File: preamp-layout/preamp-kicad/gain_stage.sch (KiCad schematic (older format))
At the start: 0 parts

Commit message: general layout work
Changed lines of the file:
@@
 $Descr A4 11693 8268
 encoding utf-8
-Sheet 11 11
+Sheet 13 13
 Title ""
 Date ""
@@
 Text HLabel 8050 3000 2    50   UnSpc ~ 0
 out_R
+Text HLabel 5700 4250 0    50   Output ~ 0
+MISO
+Text HLabel 5700 4400 0    50   Input ~ 0
+MOSI
+Text HLabel 5700 4550 0    50   Input ~ 0
+CLK
+Text HLabel 5700 4700 0    50   Input ~ 0
+CS_VOL
 $EndSCHEMATC

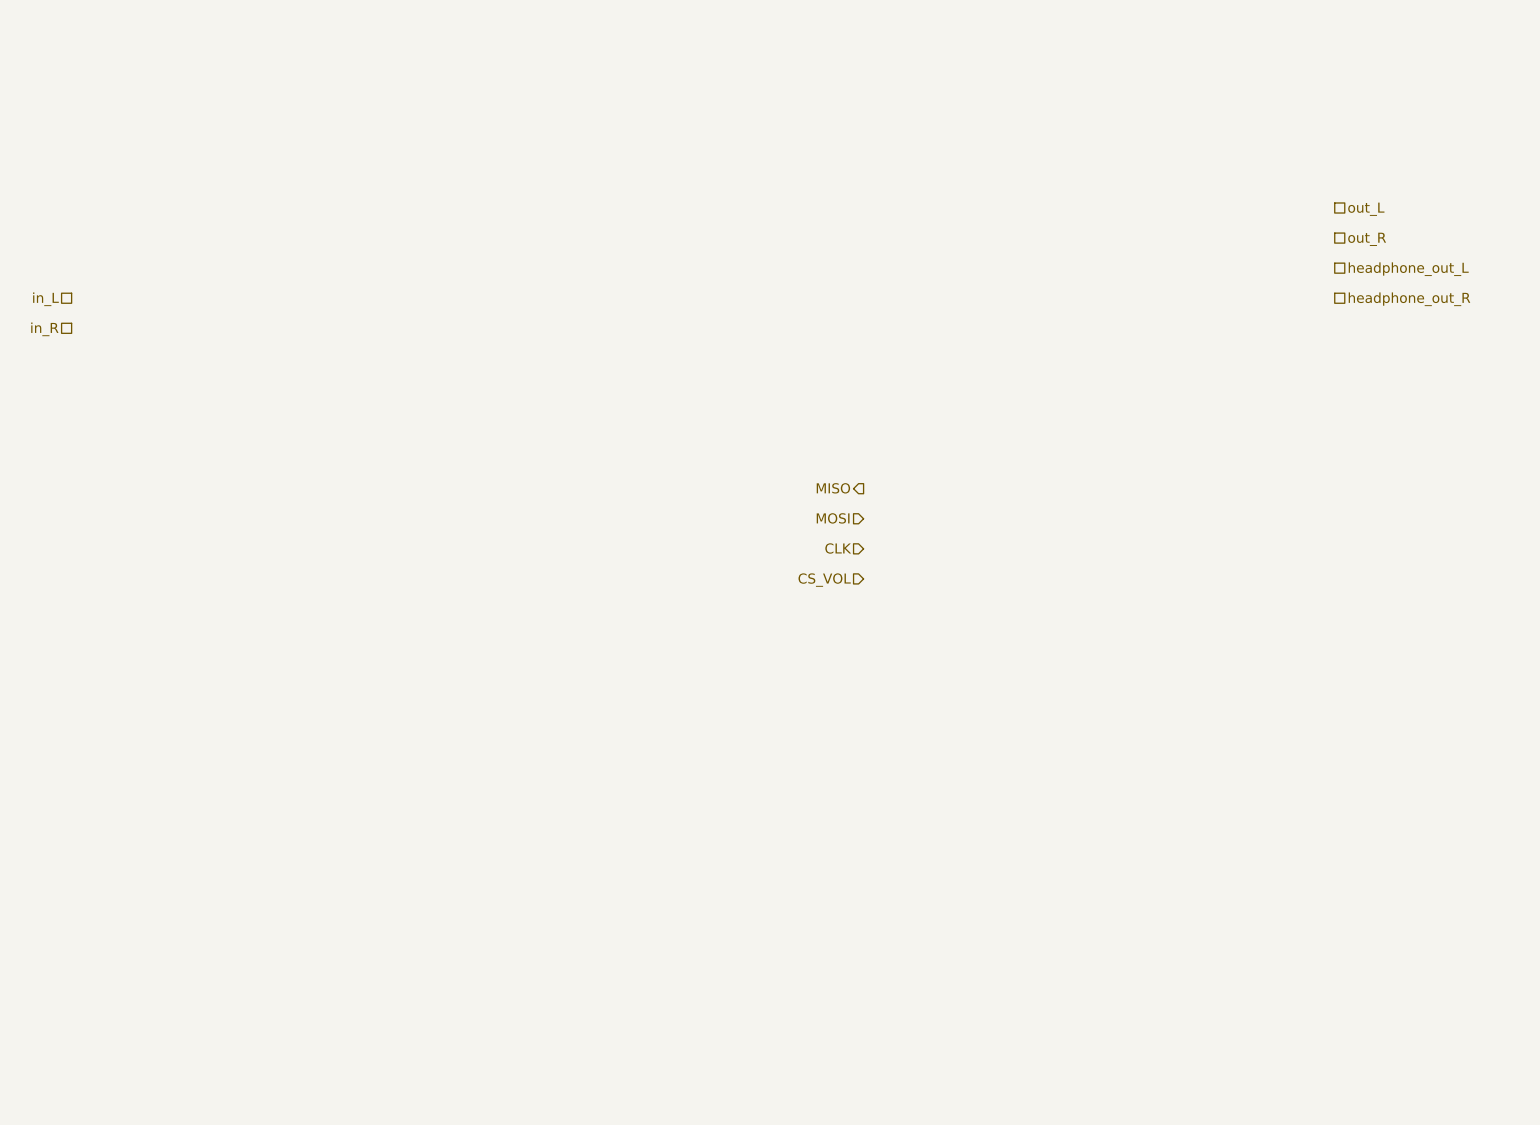
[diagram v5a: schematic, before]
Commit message: Added preliminary gain stage
Gain stage added with choice of 6db or 12db gain. Cleaned up Gain stage IO pins on preamp sheet. Broke out volume ctrl to its own board, updated accordingly. Minor routing changes on preamp sheet.
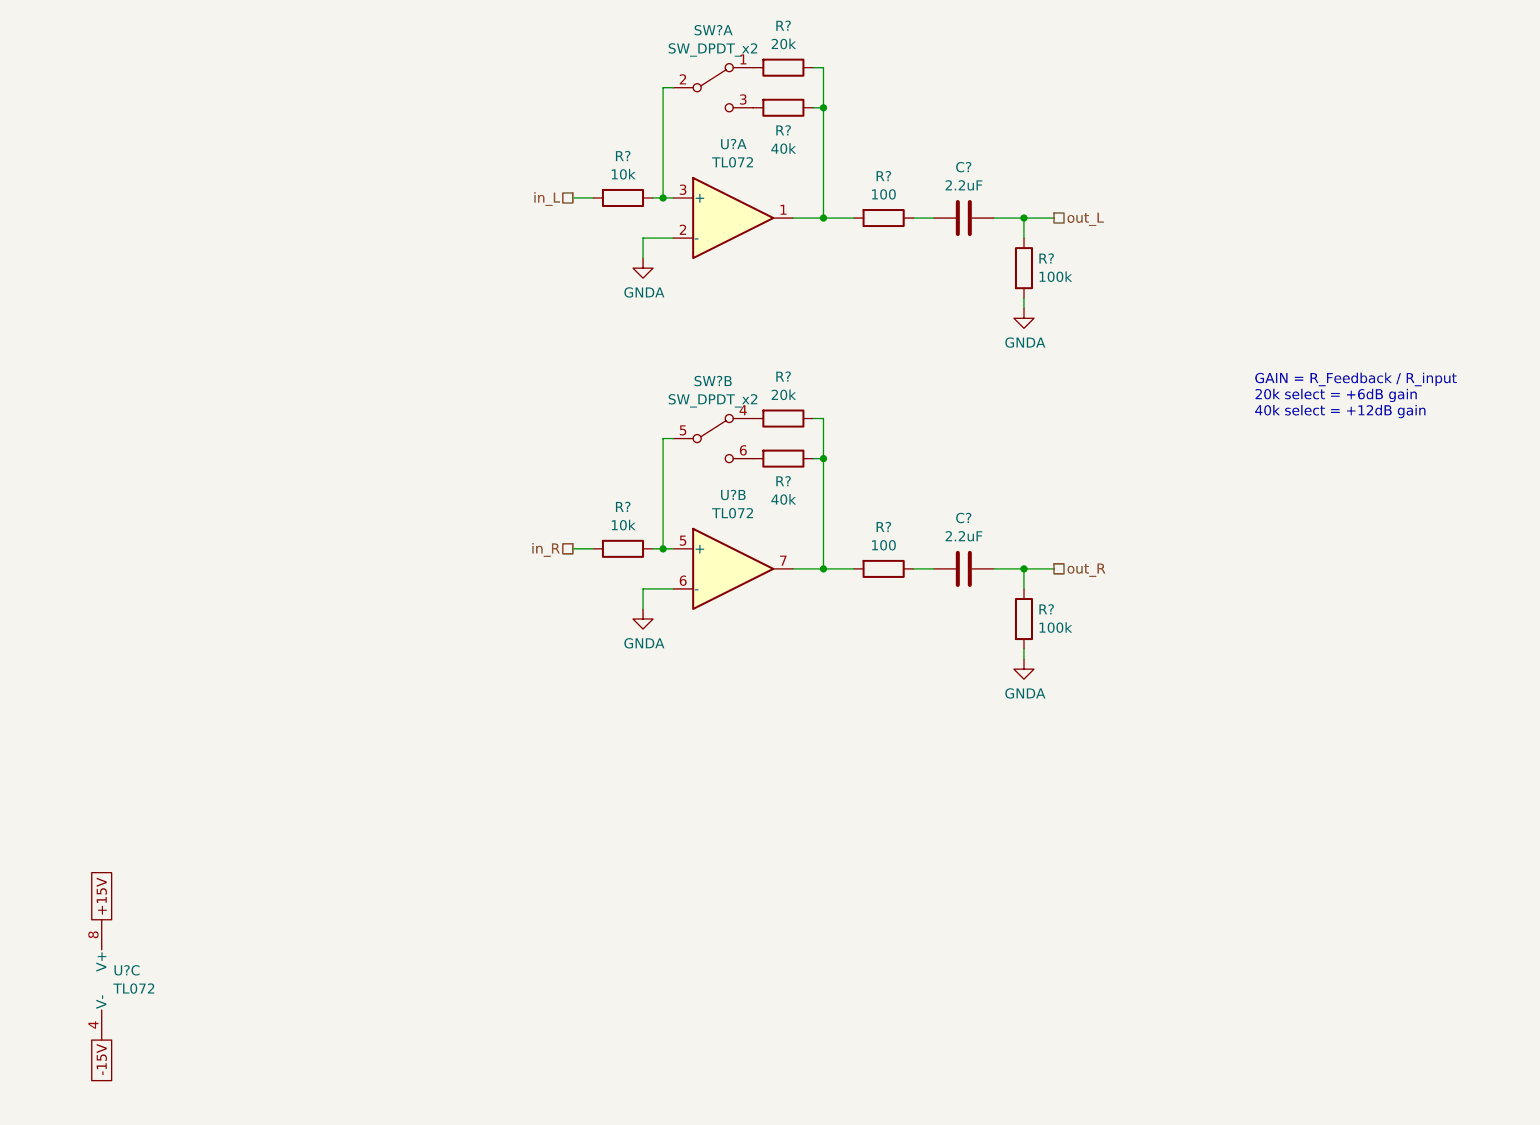
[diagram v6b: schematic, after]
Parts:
- added C? (x2): 2.2uF, symbol Device:C
- added R? (x2): 100, symbol Device:R
- added R? (x2): 100k, symbol Device:R
- added R? (x2): 40k, symbol Device:R
- added R? (x2): 10k, symbol Device:R
- added R? (x2): 20k, symbol Device:R
- added SW? (x2): SW_DPDT_x2, symbol Switch:SW_DPDT_x2
- added U? (x3): TL072, symbol Amplifier_Operational:TL072
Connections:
- net in_L: now also R?.2
- net in_R: now also R?.2
- net out_L: now also C?.1, R?.1
- net out_R: now also C?.1, R?.1
- new net: R?.1, SW?.5 (B), U?.5 (+)
- new net: R?.1, R?.1, R?.2, U?.7
- new net: R?.1, R?.1, R?.2, U?.1
- new net: R?.1, SW?.2 (B), U?.3 (+)
- new net: C?.2, R?.1 (x2)
- new net: R?.2, SW?.6 (C)
- new net: R?.2, SW?.4 (A)
- new net: R?.2, SW?.1 (A)
- new net: R?.2, SW?.3 (C)
- new net +15V: U?.8 (V+)
- new net -15V: U?.4 (V-)
- new net GNDA: R?.2, R?.2, U?.2 (-), U?.6 (-)
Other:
- note added: "GAIN = R_Feedback / R_input\n20k select = +6dB gain\n40k select = +12dB gain"
